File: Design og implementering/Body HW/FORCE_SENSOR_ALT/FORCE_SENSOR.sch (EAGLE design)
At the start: 15 parts, among them IC1 MCP6004P, J1 RJ11-6PTH, J2 RJ11-6PTH

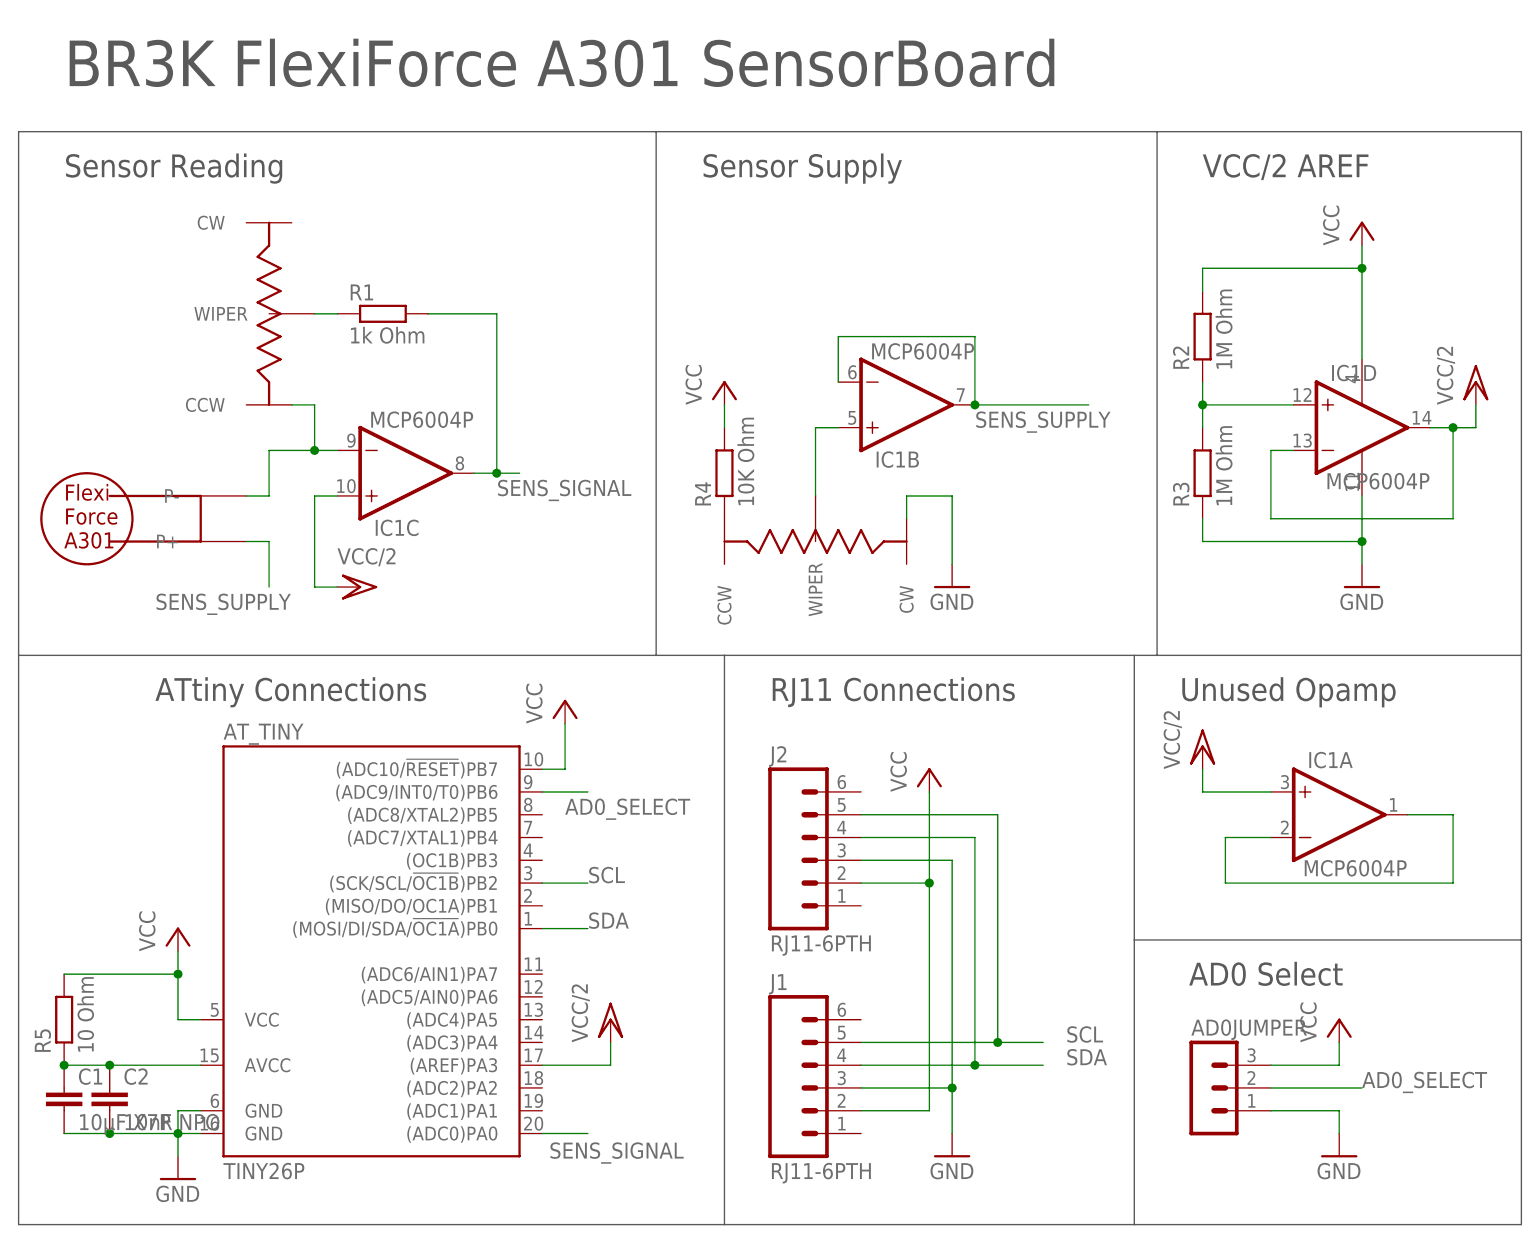
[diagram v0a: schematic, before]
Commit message: Added improved Force sensor design -Felix
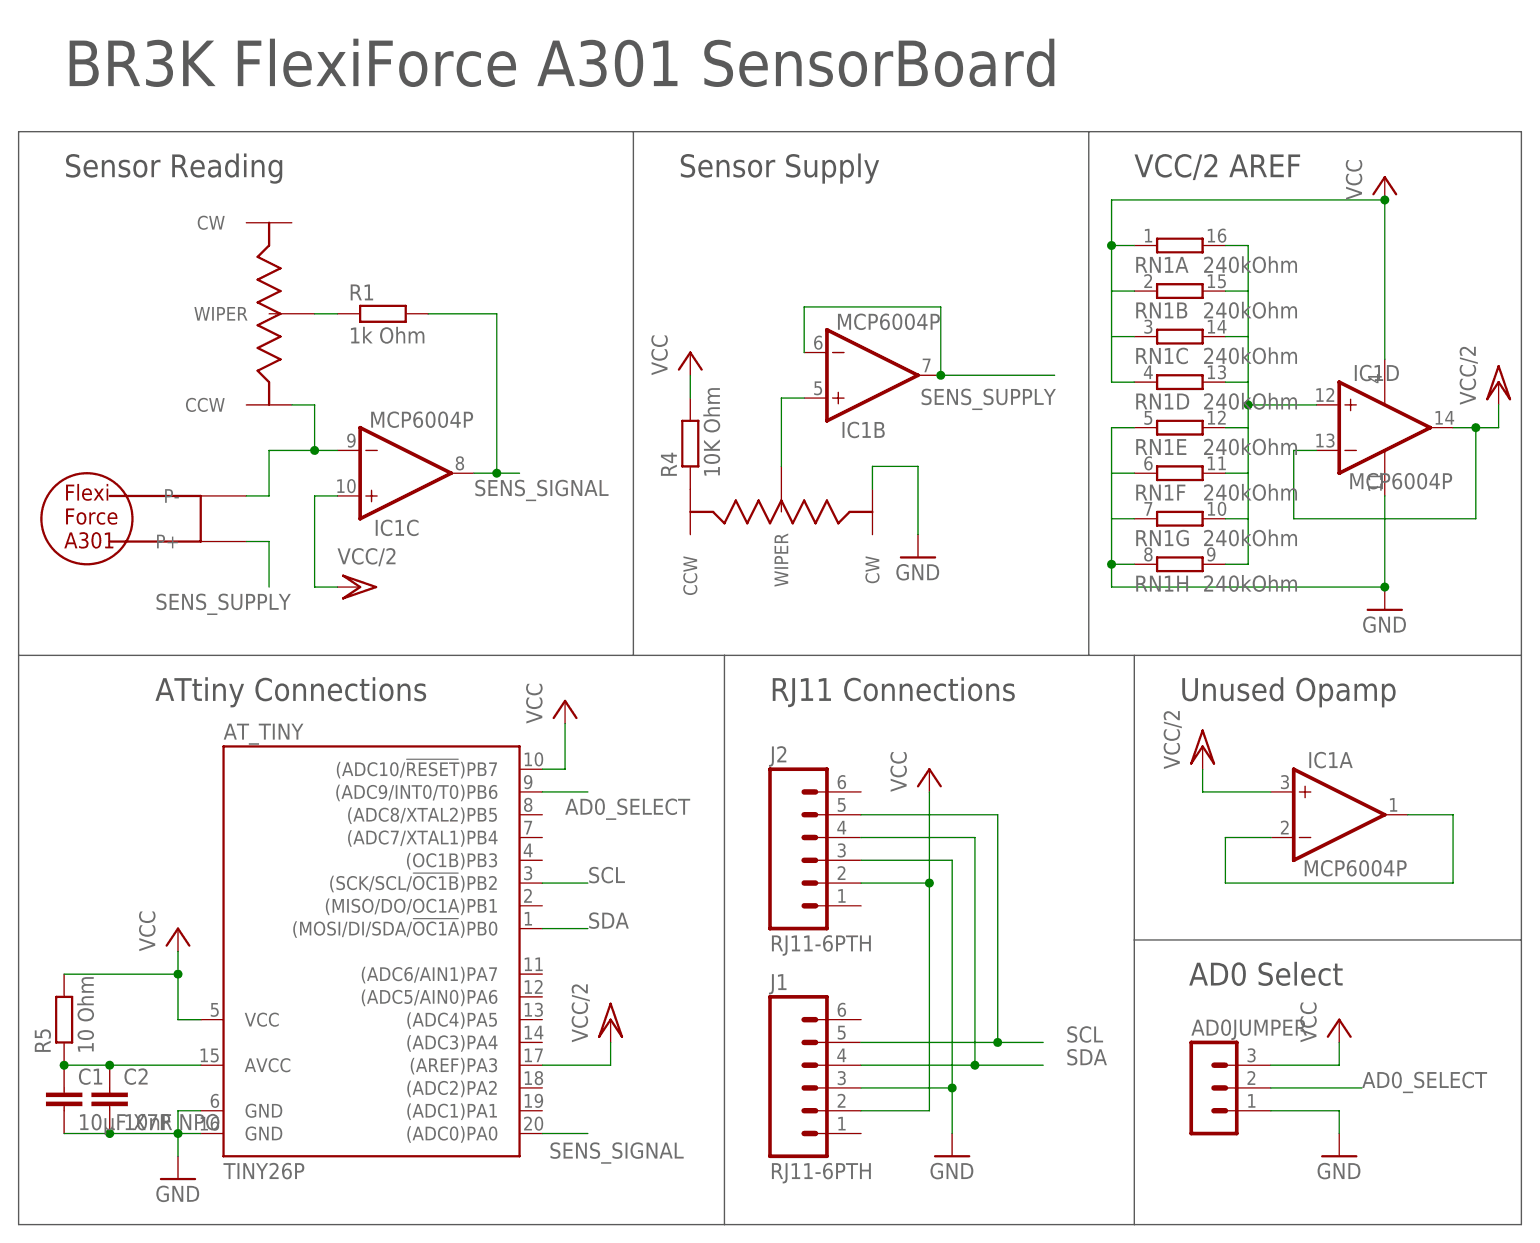
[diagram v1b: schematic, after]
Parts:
- removed R2, R3: 1M Ohm, resistor:R-EU_0207_10
- added RN1: 240kOhm, resistor-dil:8R-N
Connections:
- removed net N$2: IC1D.+IN, R2.1, R3.2
- new net N$11: IC1D.+IN, RN1A.2, RN1B.2, RN1C.2, RN1D.2, RN1E.2, RN1F.2, RN1G.2, RN1H.2
- net GND: now also RN1E.1, RN1F.1, RN1G.1, RN1H.1; no longer R3.1
- net VCC: now also RN1A.1, RN1B.1, RN1C.1, RN1D.1; no longer R2.2
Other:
- moved on the sheet: IC1B, IC1D, R4
